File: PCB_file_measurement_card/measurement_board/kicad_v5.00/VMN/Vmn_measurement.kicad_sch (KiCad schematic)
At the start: 19 parts, among them J3 Screw_Terminal_VMN, U2 INA128, U3 LM358, U4 1085-Adress=0X48

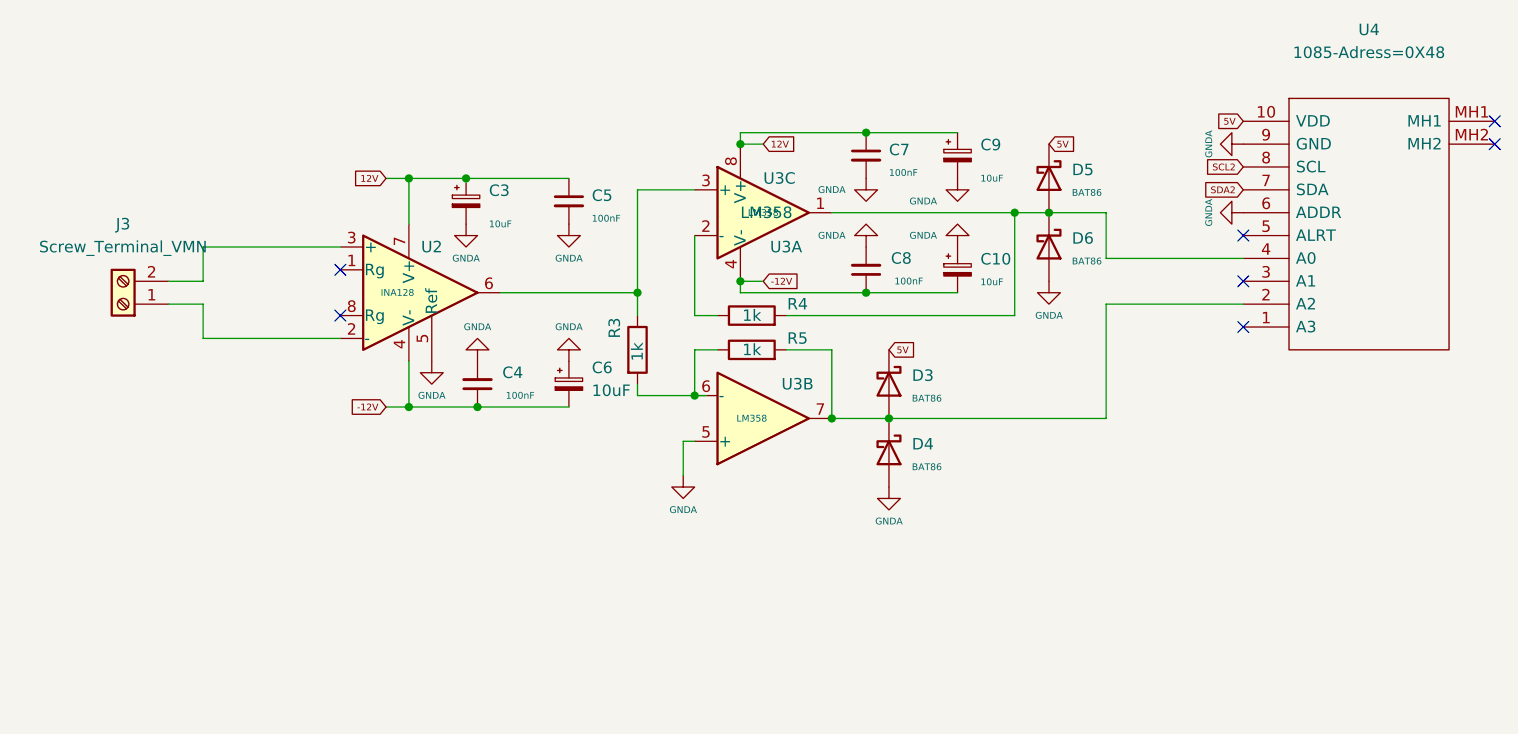
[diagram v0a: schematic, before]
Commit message: new schematics for V5.00
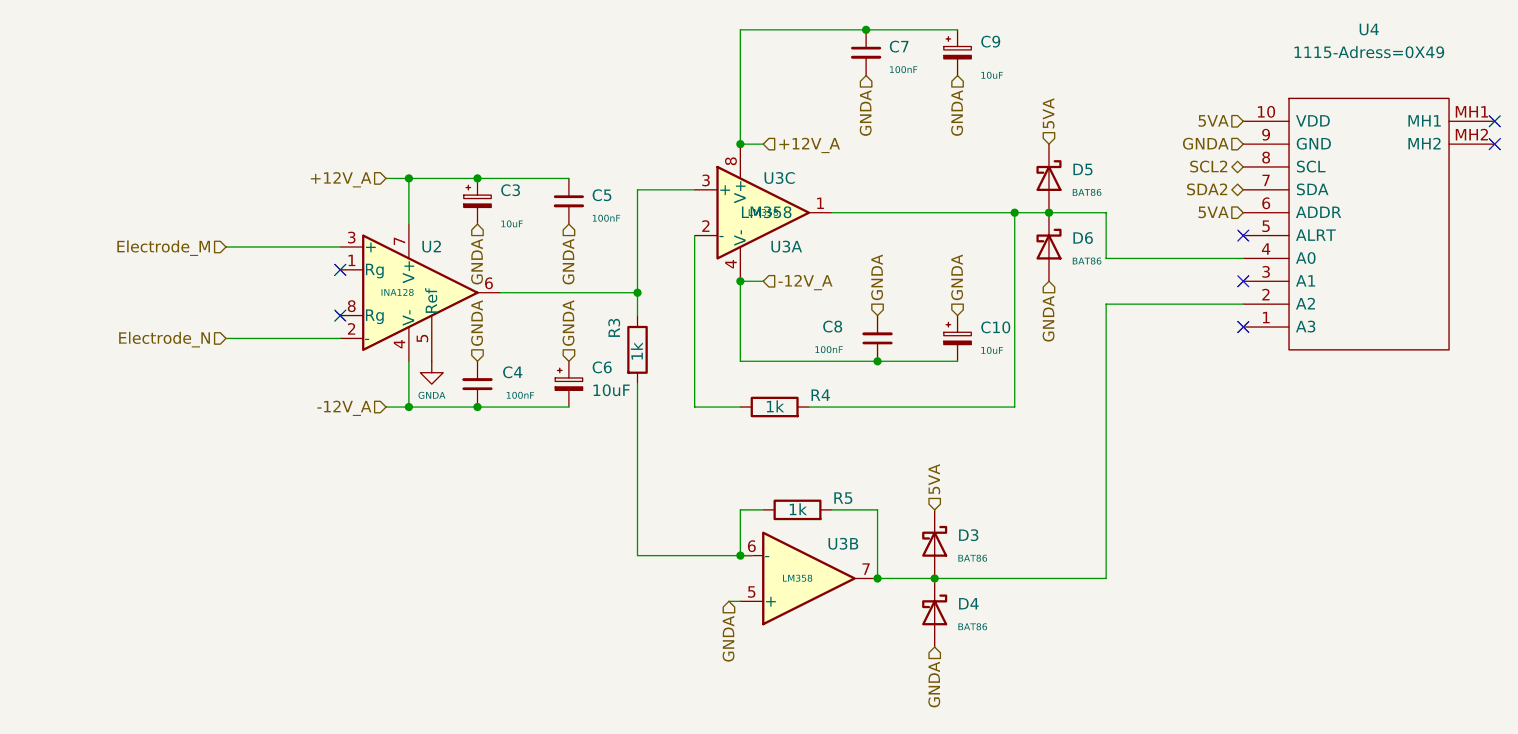
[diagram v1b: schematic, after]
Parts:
- removed J3: Screw_Terminal_VMN, TerminalBlock_Phoenix:TerminalBlock_Phoenix_MKDS-1,5-2-5.08_1x02_P5.08mm_Horizontal, symbol Connector:Screw_Terminal_01x02
- U4: value 1085-Adress=0X48 -> 1115-Adress=0X49
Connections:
- net GNDA: no longer U4.6 (ADDR)
- net Electrode_N: now reaches U2.2 (-)
- net Electrode_M: now reaches U2.3 (+)
- net -12V renamed -12V_A
- net 12V renamed +12V_A
- net 5V renamed 5VA
- net 5VA: now also U4.6 (ADDR)
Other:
- moved on the sheet: C10, C3, C7, C8, C9, D3, D4, R4, R5, U3B

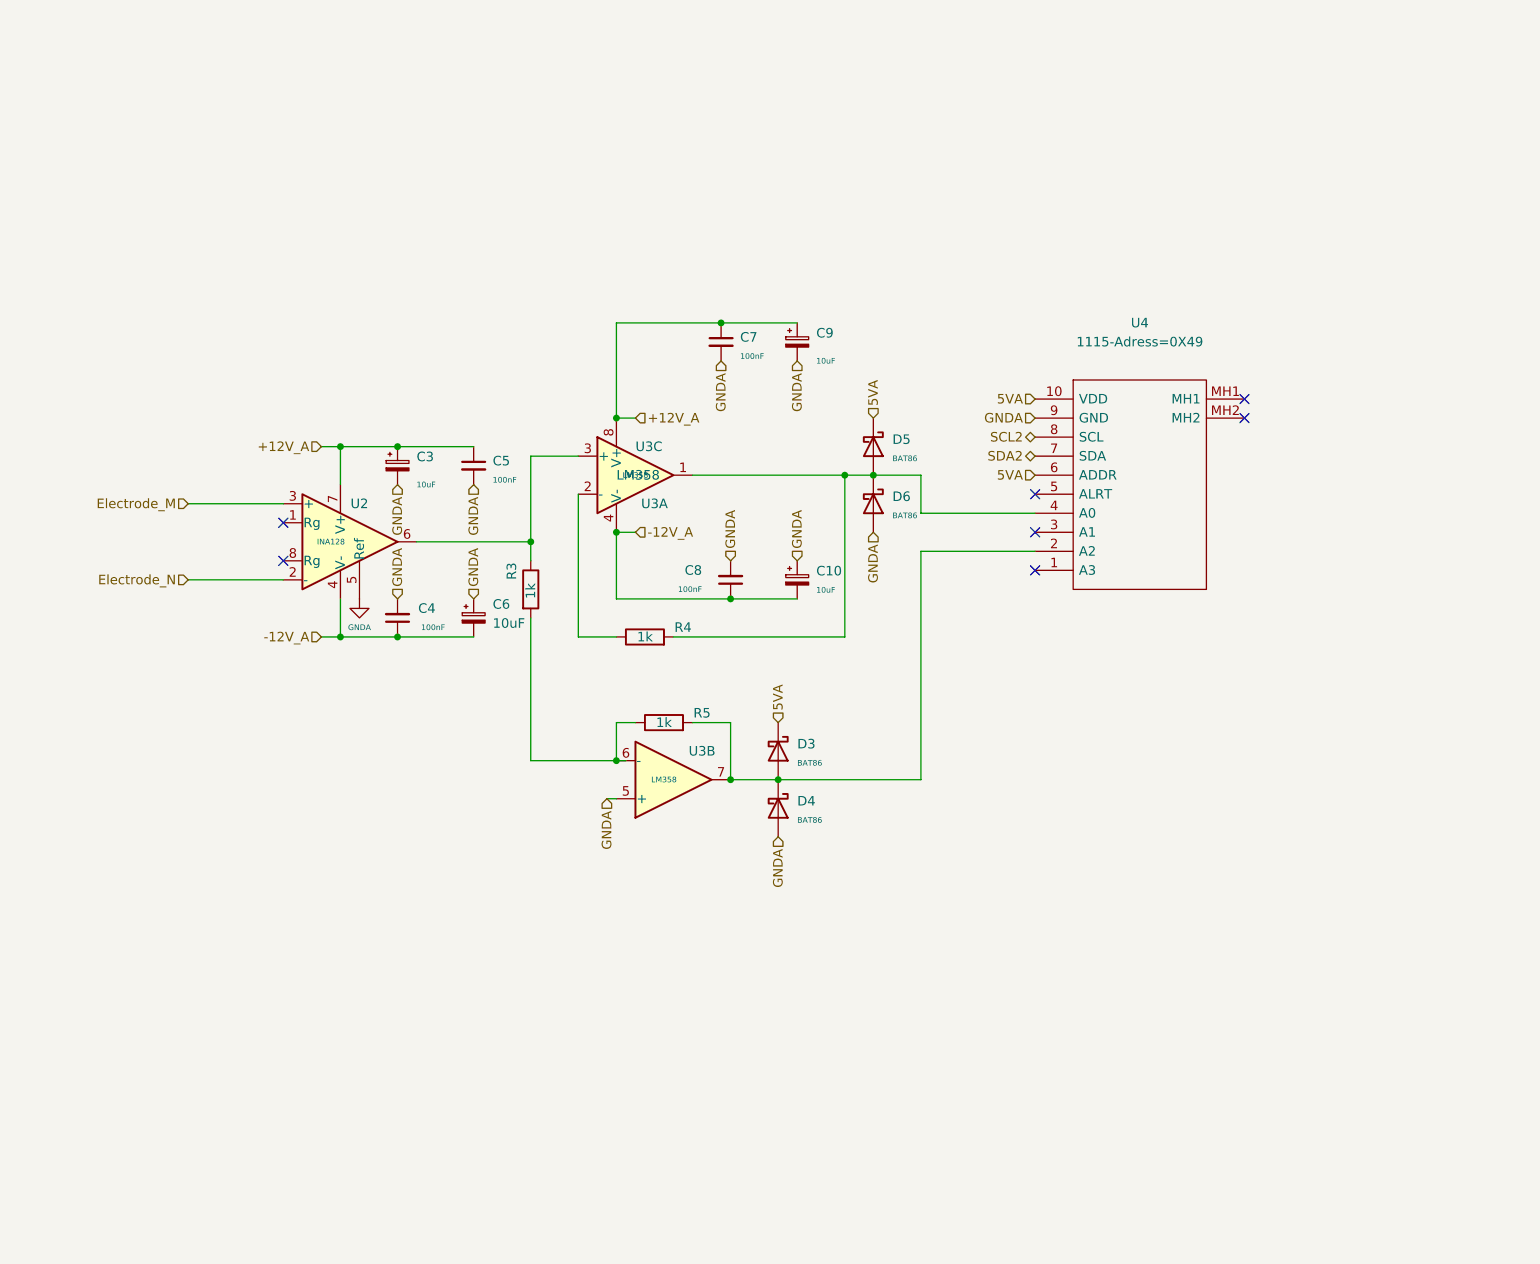
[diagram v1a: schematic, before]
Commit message: new measurement board
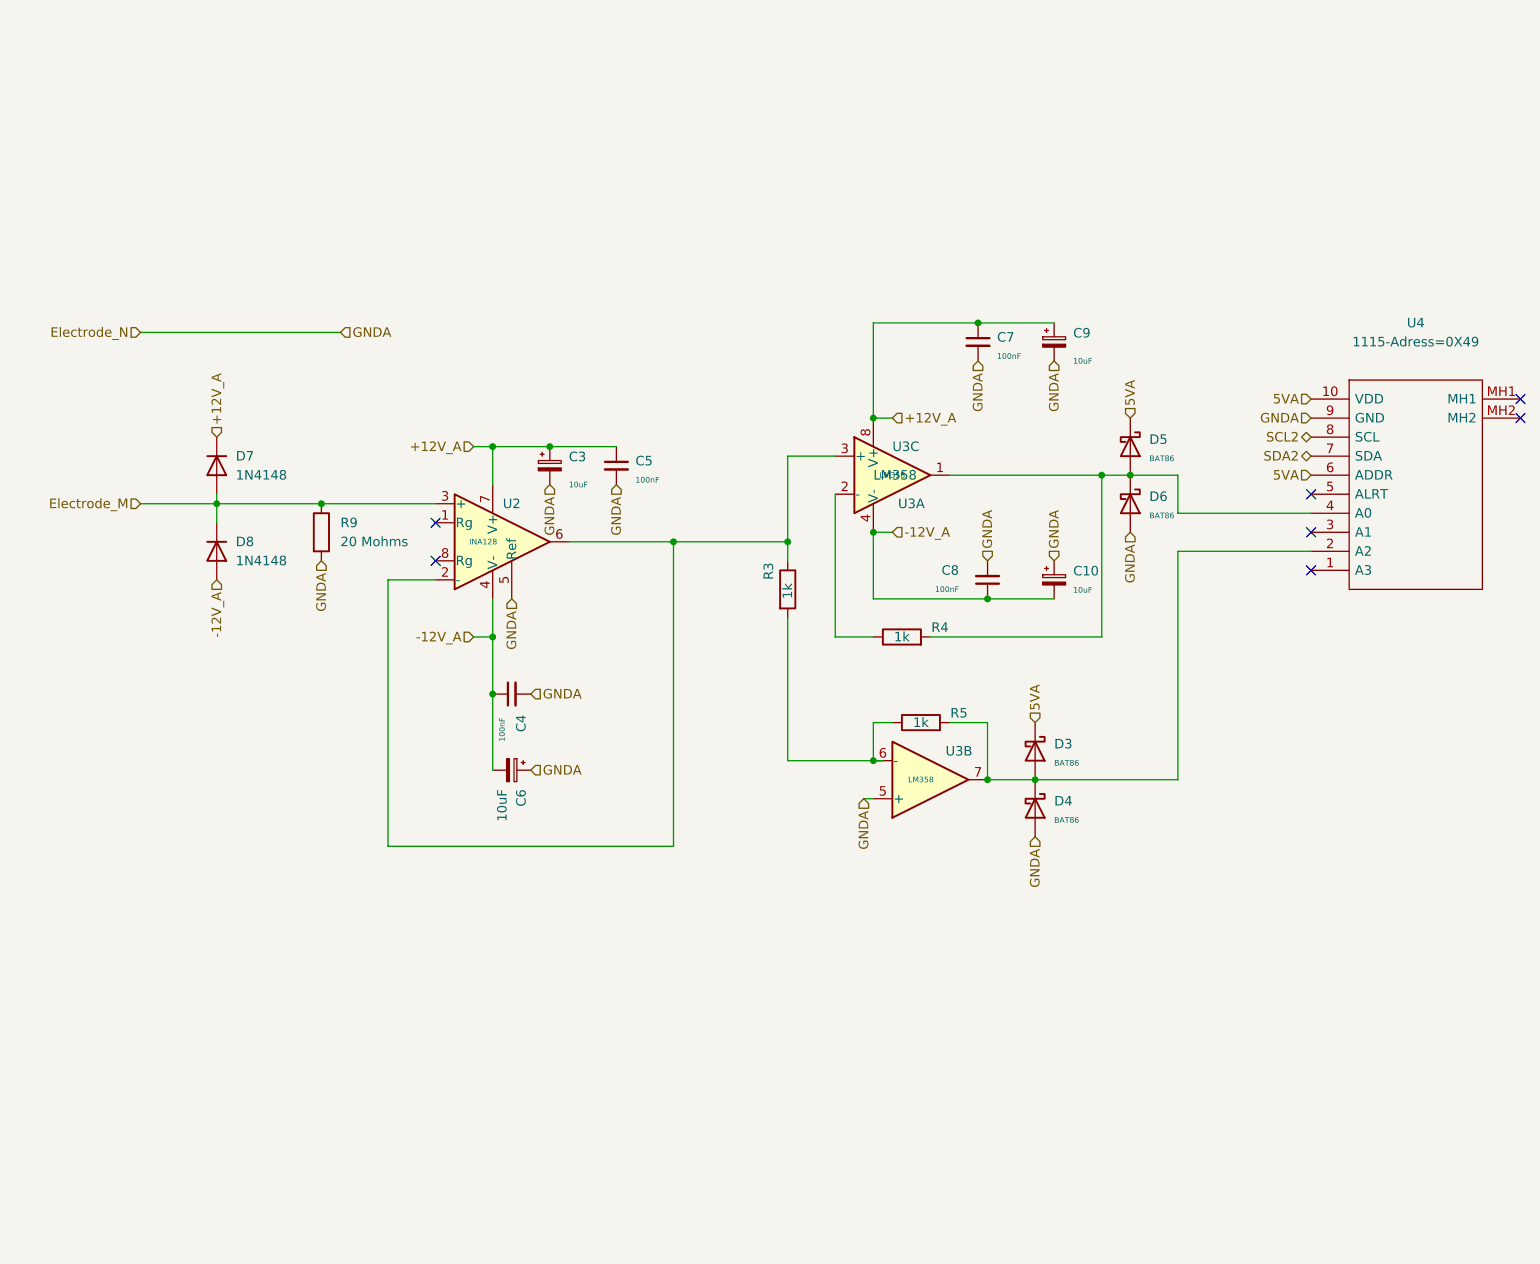
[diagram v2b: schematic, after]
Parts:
- added D7, D8: 1N4148, Diode_THT:D_DO-35_SOD27_P7.62mm_Horizontal, symbol Diode:1N4148
- added R9: 20 Mohms, Resistor_THT:R_Axial_DIN0204_L3.6mm_D1.6mm_P7.62mm_Horizontal, symbol Device:R
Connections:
- net GNDA is gone; now on net Electrode_N: C10.1, C3.2, C4.2, C5.2, C6.1, C7.2, C8.2, C9.2, D4.2 (A), D6.2 (A), U2.5 (Ref), U3.5 (+), U4.9 (GND)
- net +12V_A: now also D7.1 (K)
- net -12V_A: now also D8.2 (A)
- net Electrode_M: now also D7.2 (A), D8.1 (K), R9.1
- net Electrode_N: now also R9.2; no longer U2.2 (-)
- net at R3.1, U2.6, U3.3 (+): now also U2.2 (-)
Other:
- moved on the sheet: C10, C3, C4, C5, C6, C7, C8, C9, D3, D4, D5, D6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

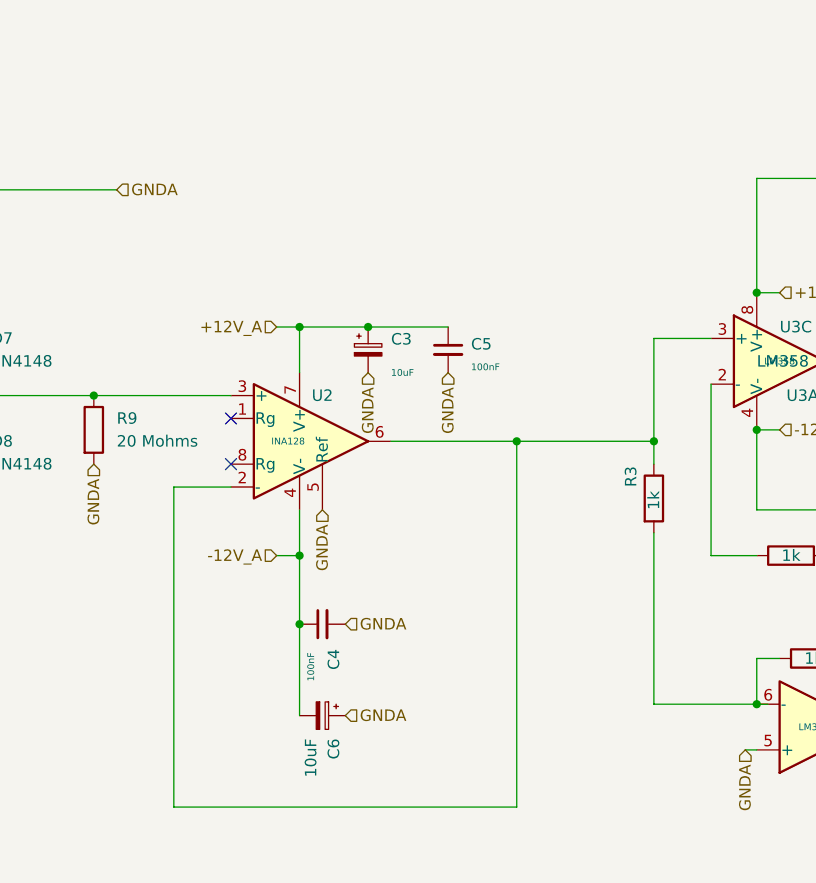
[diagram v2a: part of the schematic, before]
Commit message: remplacement INA128 par TL082carte maesure
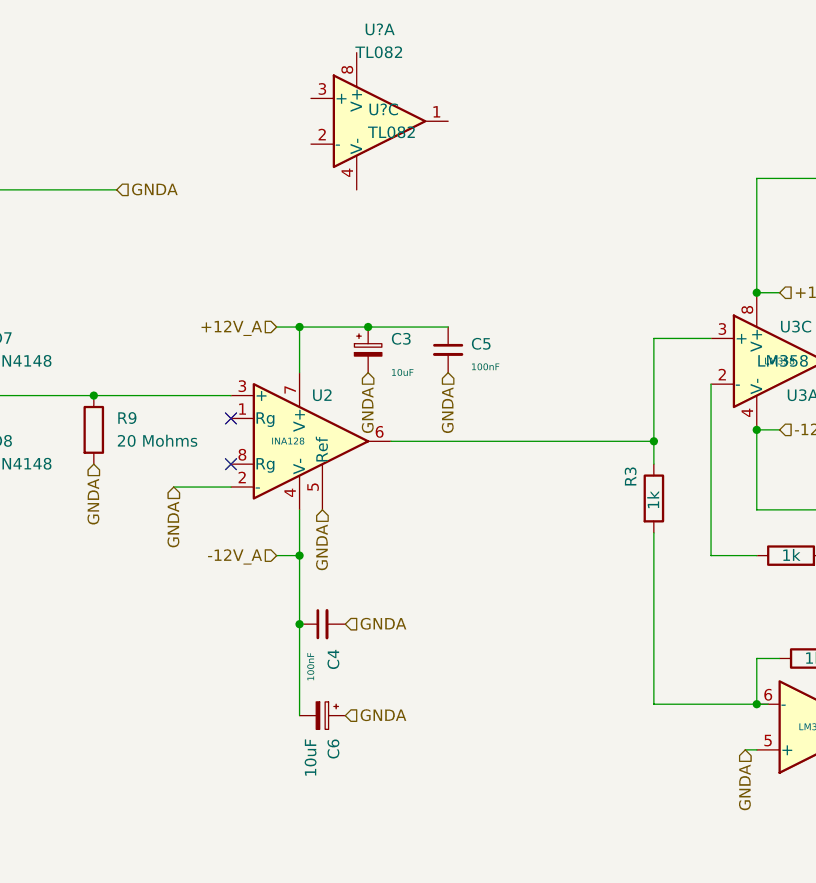
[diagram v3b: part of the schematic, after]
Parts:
- added U? (x2): TL082, symbol Amplifier_Operational:TL082
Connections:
- net Electrode_N: now also U2.2 (-)
- net at R3.1, U2.6, U3.3 (+): no longer U2.2 (-)
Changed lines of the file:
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@@
   (junction (at 54.61 97.79) (diameter 0) (color 0 0 0 0)
-  )
-  (junction (at 115.57 102.87) (diameter 0) (color 0 0 0 0)
   )
   (junction (at 130.81 102.87) (diameter 0) (color 0 0 0 0)
@@
     (stroke (width 0) (type default) (color 0 0 0 0))
   )
-  (wire (pts (xy 115.57 102.87) (xy 115.57 143.51))
-    (stroke (width 0) (type default) (color 0 0 0 0))
-  )
   (wire (pts (xy 91.44 110.49) (xy 91.44 115.57))
     (stroke (width 0) (type default) (color 0 0 0 0))
   )
-  (wire (pts (xy 77.47 107.95) (xy 77.47 143.51))
-    (stroke (width 0) (type default) (color 0 0 0 0))
-  )
   (wire (pts (xy 200.66 104.14) (xy 182.88 104.14))
     (stroke (width 0) (type default) (color 0 0 0 0))
@@
     (stroke (width 0) (type default) (color 0 0 0 0))
   )
-  (wire (pts (xy 77.47 143.51) (xy 115.57 143.51))
-    (stroke (width 0) (type default) (color 0 0 0 0))
-  )
-  (wire (pts (xy 101.6 102.87) (xy 115.57 102.87))
+  (wire (pts (xy 101.6 102.87) (xy 130.81 102.87))
     (stroke (width 0) (type default) (color 0 0 0 0))
   )
@@
     (stroke (width 0) (type default) (color 0 0 0 0))
   )
-  (wire (pts (xy 115.57 102.87) (xy 130.81 102.87))
-    (stroke (width 0) (type default) (color 0 0 0 0))
-  )
   (wire (pts (xy 54.61 97.79) (xy 68.58 97.79))
     (stroke (width 0) (type default) (color 0 0 0 0))
@@
   )
   (hierarchical_label "GNDA" (shape input) (at 68.58 105.41 270)
+    (effects (font (size 1.27 1.27)) (justify right))
+  )
+  (hierarchical_label "GNDA" (shape input) (at 77.47 107.95 270)
     (effects (font (size 1.27 1.27)) (justify right))
   )
@@
     (pin "MH2")
   )
+  (symbol (lib_id "Amplifier_Operational:TL082") (at 100.33 67.31 0) (unit 1)
+    (in_bom yes) (on_board yes) (fields_autoplaced)
+    (property "Reference" "U?" (id 0) (at 100.33 57.15 0))
+    (property "Value" "TL082" (id 1) (at 100.33 59.69 0))
+    (property "Footprint" "" (id 2) (at 100.33 67.31 0)
+      (effects (font (size 1.27 1.27)) hide)
+    )
+    (property "Datasheet" "http://www.ti.com/lit/ds/symlink/tl081.pdf" (id 3) (at 100.33 67.31 0)
+      (effects (font (size 1.27 1.27)) hide)
+    )
+    (pin "1")
+    (pin "2")
+    (pin "3")
+    (pin "5")
+    (pin "6")
+    (pin "7")
+    (pin "4")
+    (pin "8")
+  )
   (symbol (lib_id "Device:R") (at 148.59 127 90) (unit 1)
     (in_bom yes) (on_board yes)
@@
     (pin "2")
   )
+  (symbol (lib_id "Amplifier_Operational:TL082") (at 100.33 67.31 0) (unit 3)
+    (in_bom yes) (on_board yes) (fields_autoplaced)
+    (property "Reference" "U?" (id 0) (at 99.06 66.0399 0)
+      (effects (font (size 1.27 1.27)) (justify left))
+    )
+    (property "Value" "TL082" (id 1) (at 99.06 68.5799 0)
+      (effects (font (size 1.27 1.27)) (justify left))
+    )
+    (property "Footprint" "" (id 2) (at 100.33 67.31 0)
+      (effects (font (size 1.27 1.27)) hide)
+    )
+    (property "Datasheet" "http://www.ti.com/lit/ds/symlink/tl081.pdf" (id 3) (at 100.33 67.31 0)
+      (effects (font (size 1.27 1.27)) hide)
+    )
+    (pin "1")
+    (pin "2")
+    (pin "3")
+    (pin "5")
+    (pin "6")
+    (pin "7")
+    (pin "4")
+    (pin "8")
+  )
   (symbol (lib_id "Device:R") (at 68.58 101.6 0) (unit 1)

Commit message: new version of measurement board
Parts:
- removed U? (x2): TL082, symbol Amplifier_Operational:TL082
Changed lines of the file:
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@@
     (stroke (width 0) (type default) (color 0 0 0 0))
   )
-  (wire (pts (xy 44.45 74.93) (xy 71.12 74.93))
+  (wire (pts (xy 44.45 125.73) (xy 71.12 125.73))
     (stroke (width 0) (type default) (color 0 0 0 0))
   )
@@
     (effects (font (size 1.27 1.27)) (justify left))
   )
-  (hierarchical_label "GNDA" (shape input) (at 71.12 74.93 0)
+  (hierarchical_label "GNDA" (shape input) (at 71.12 125.73 0)
     (effects (font (size 1.27 1.27)) (justify left))
   )
@@
     (effects (font (size 1.27 1.27)) (justify right))
   )
-  (hierarchical_label "Electrode_N" (shape input) (at 44.45 74.93 180)
+  (hierarchical_label "Electrode_N" (shape input) (at 44.45 125.73 180)
     (effects (font (size 1.27 1.27)) (justify right))
   )
@@
     (pin "MH2")
   )
-  (symbol (lib_id "Amplifier_Operational:TL082") (at 100.33 67.31 0) (unit 1)
-    (in_bom yes) (on_board yes) (fields_autoplaced)
-    (property "Reference" "U?" (id 0) (at 100.33 57.15 0))
-    (property "Value" "TL082" (id 1) (at 100.33 59.69 0))
-    (property "Footprint" "" (id 2) (at 100.33 67.31 0)
-      (effects (font (size 1.27 1.27)) hide)
-    )
-    (property "Datasheet" "http://www.ti.com/lit/ds/symlink/tl081.pdf" (id 3) (at 100.33 67.31 0)
-      (effects (font (size 1.27 1.27)) hide)
-    )
-    (pin "1")
-    (pin "2")
-    (pin "3")
-    (pin "5")
-    (pin "6")
-    (pin "7")
-    (pin "4")
-    (pin "8")
-  )
   (symbol (lib_id "Device:R") (at 148.59 127 90) (unit 1)
     (in_bom yes) (on_board yes)
@@
     (pin "2")
   )
-  (symbol (lib_id "Amplifier_Operational:TL082") (at 100.33 67.31 0) (unit 3)
-    (in_bom yes) (on_board yes) (fields_autoplaced)
-    (property "Reference" "U?" (id 0) (at 99.06 66.0399 0)
-      (effects (font (size 1.27 1.27)) (justify left))
-    )
-    (property "Value" "TL082" (id 1) (at 99.06 68.5799 0)
-      (effects (font (size 1.27 1.27)) (justify left))
-    )
-    (property "Footprint" "" (id 2) (at 100.33 67.31 0)
-      (effects (font (size 1.27 1.27)) hide)
-    )
-    (property "Datasheet" "http://www.ti.com/lit/ds/symlink/tl081.pdf" (id 3) (at 100.33 67.31 0)
-      (effects (font (size 1.27 1.27)) hide)
-    )
-    (pin "1")
-    (pin "2")
-    (pin "3")
-    (pin "5")
-    (pin "6")
-    (pin "7")
-    (pin "4")
-    (pin "8")
-  )
   (symbol (lib_id "Device:R") (at 68.58 101.6 0) (unit 1)
